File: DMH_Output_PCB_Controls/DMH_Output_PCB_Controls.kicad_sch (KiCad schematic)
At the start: 14 parts, among them J1 TS_Jack_6.35mm_Sw, J2 TS_Jack_6.35mm_Sw, J200 IDC_02x05, J21 Conn_01x02, J22 Conn_01x02, J24 Conn_01x02, J25 Conn_01x02, J3 TRS Jack 6.35mm, J4 TRS Jack 6.35mm, J5 TRS Jack 6.35mm, J6 TS_Jack_6.35mm_Sw, J7 TS_Jack_6.35mm_Sw, J8 TS_Jack_6.35mm_Sw, J9 TS_Jack_6.35mm_Sw

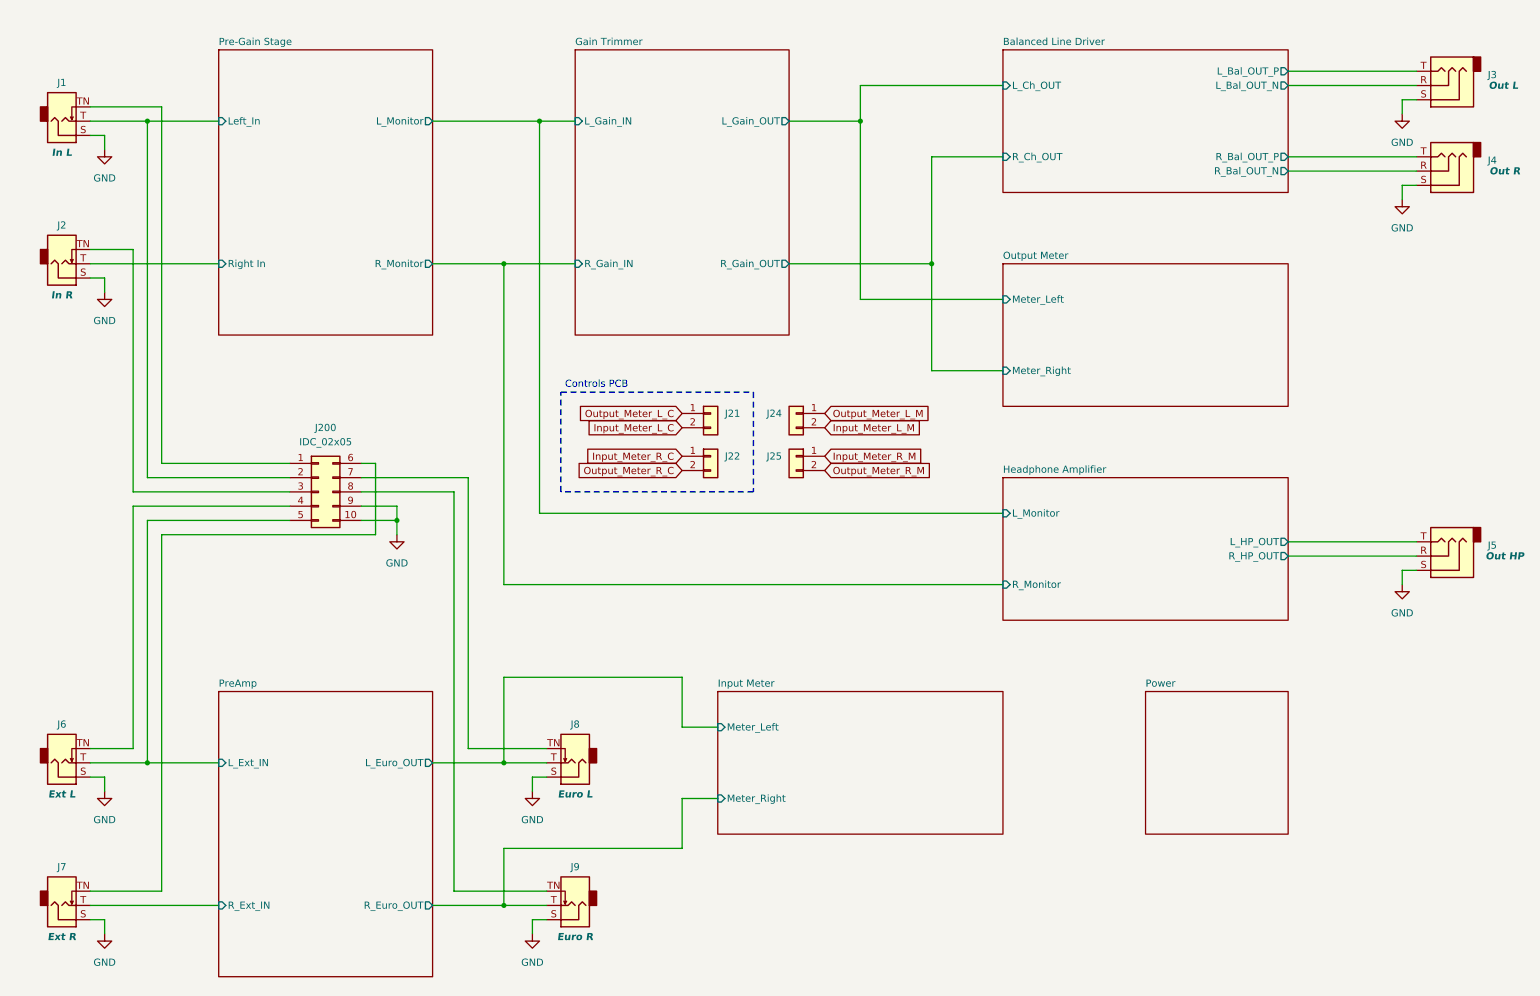
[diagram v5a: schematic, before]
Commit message: Replaced jack symbols with 5pin ones
Also updated Meter LED current source resistor to 75R
Also increased LED guiding PCB mounting holes to M2.5
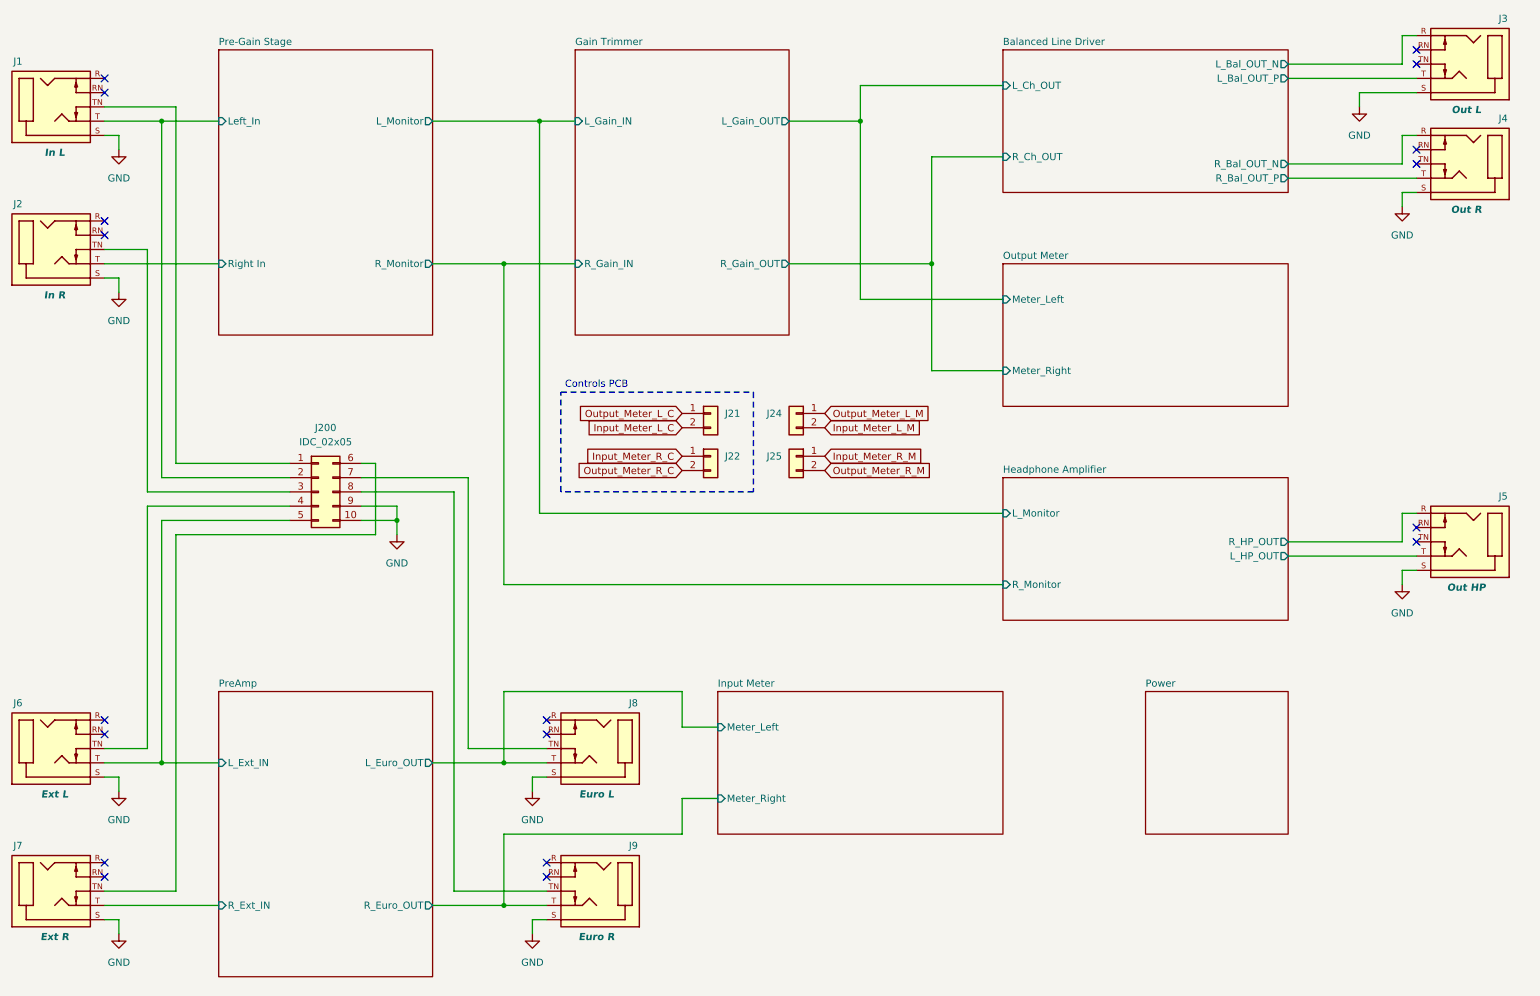
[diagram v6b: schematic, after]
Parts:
- removed J1, J2, J6, J7, J8, J9: TS_Jack_6.35mm_Sw, SynthStuff:CUI_MJ-63052A, symbol SynthStuff:TS_Jack_6.35mm_Sw
- removed J3, J4, J5: TRS Jack 6.35mm, SynthStuff:CUI_SJ-63083A, symbol Connector_Audio:AudioJack3
- added J1, J2, J3, J4, J5, J6, J7, J8, J9: TRS_Jack_6.35mm_Sw, SynthStuff:CUI_SJ-63083D, symbol SynthStuff:TRS_Jack_6.35mm_Sw
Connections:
- net Balanced Line Driver/L_Bal_OUT_N: now also J3.R (4)
- net Balanced Line Driver/L_Bal_OUT_P: now also J3.T (3)
- net Balanced Line Driver/R_Bal_OUT_N: now also J4.R (4)
- net Balanced Line Driver/R_Bal_OUT_P: now also J4.T (3)
- net GND: now also J1.S (1), J2.S (1), J3.S (1), J4.S (1), J5.S (1), J6.S (1), J7.S (1), J8.S (1), J9.S (1)
- net Headphone Amplifier/L_HP_OUT: now also J5.T (3)
- net Headphone Amplifier/R_HP_OUT: now also J5.R (4)
- net Input Meter/Meter_Left: now also J8.T (3)
- net Input Meter/Meter_Right: now also J9.T (3)
- net Pre-Gain Stage/Left_In: now also J1.T (3)
- net Pre-Gain Stage/Right In: now also J2.T (3)
- net PreAmp/L_Ext_IN: now also J6.T (3)
- net PreAmp/R_Ext_IN: now also J7.T (3)
- net at J200.7 (Pin_7): now also J8.TN (2)
- net at J200.3 (Pin_3): now also J2.TN (2)
- net at J200.6 (Pin_6): now also J7.TN (2)
- net at J200.4 (Pin_4): now also J6.TN (2)
- net at J200.8 (Pin_8): now also J9.TN (2)
- net at J200.1 (Pin_1): now also J1.TN (2)
- no-connect marks 0 -> 18

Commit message: Prep for Main and MZ PCBs design in progress
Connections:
- net GND: now also J200.5 (Pin_5); no longer J200.9 (Pin_9)
- net Pre-Gain Stage/Left_In: now also J200.6 (Pin_6); no longer J200.2 (Pin_2)
- net PreAmp/L_Ext_IN: now also J200.7 (Pin_7); no longer J200.5 (Pin_5)
- net at J7.TN (2): now also J200.2 (Pin_2); no longer J200.6 (Pin_6)
- net at J2.TN (2): now also J200.1 (Pin_1); no longer J200.3 (Pin_3)
- net at J9.TN (2): now also J200.9 (Pin_9); no longer J200.8 (Pin_8)
- net at J1.TN (2): now also J200.3 (Pin_3); no longer J200.1 (Pin_1)
- net at J8.TN (2): now also J200.8 (Pin_8); no longer J200.7 (Pin_7)

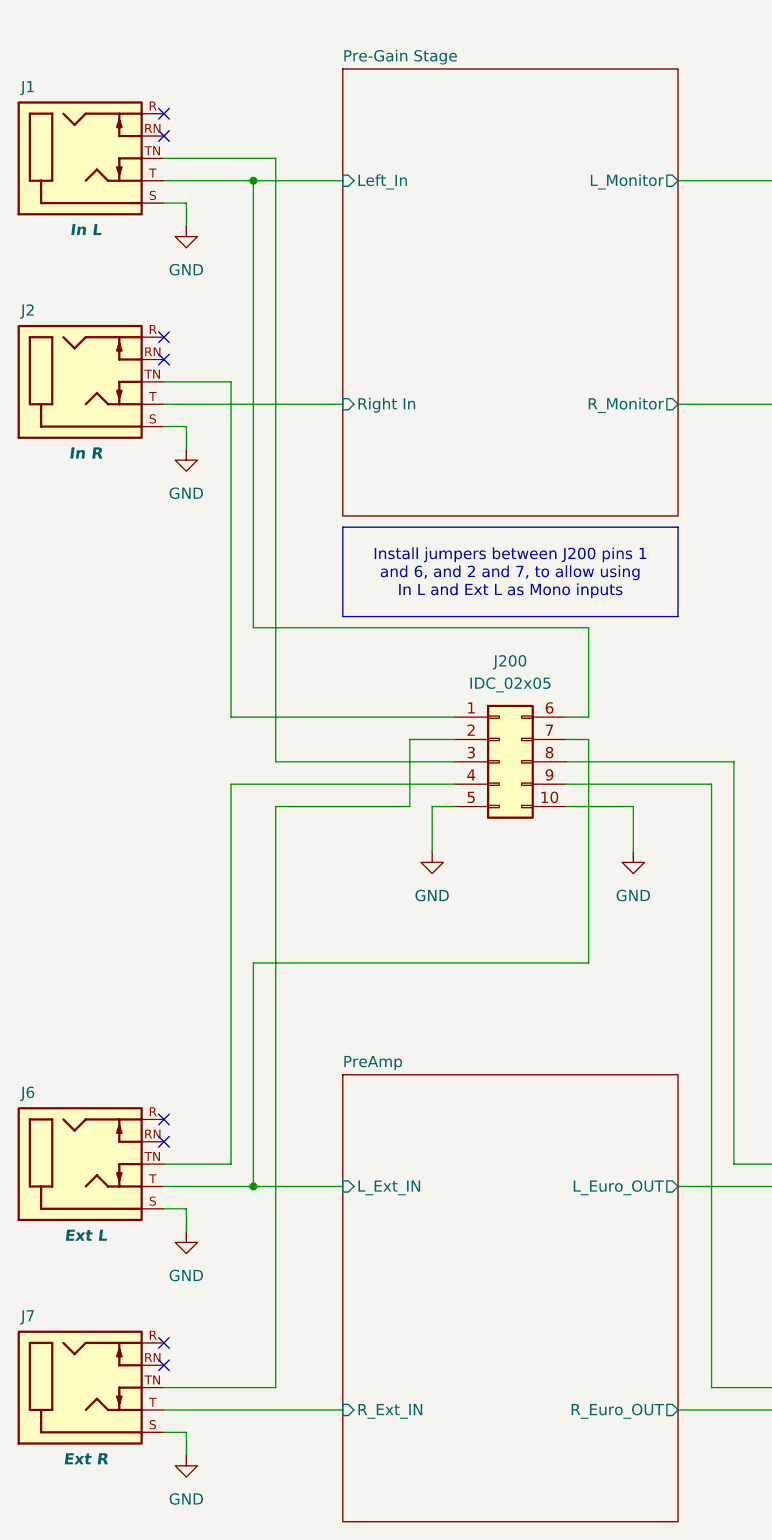
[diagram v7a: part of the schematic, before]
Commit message: Main PCB routing done
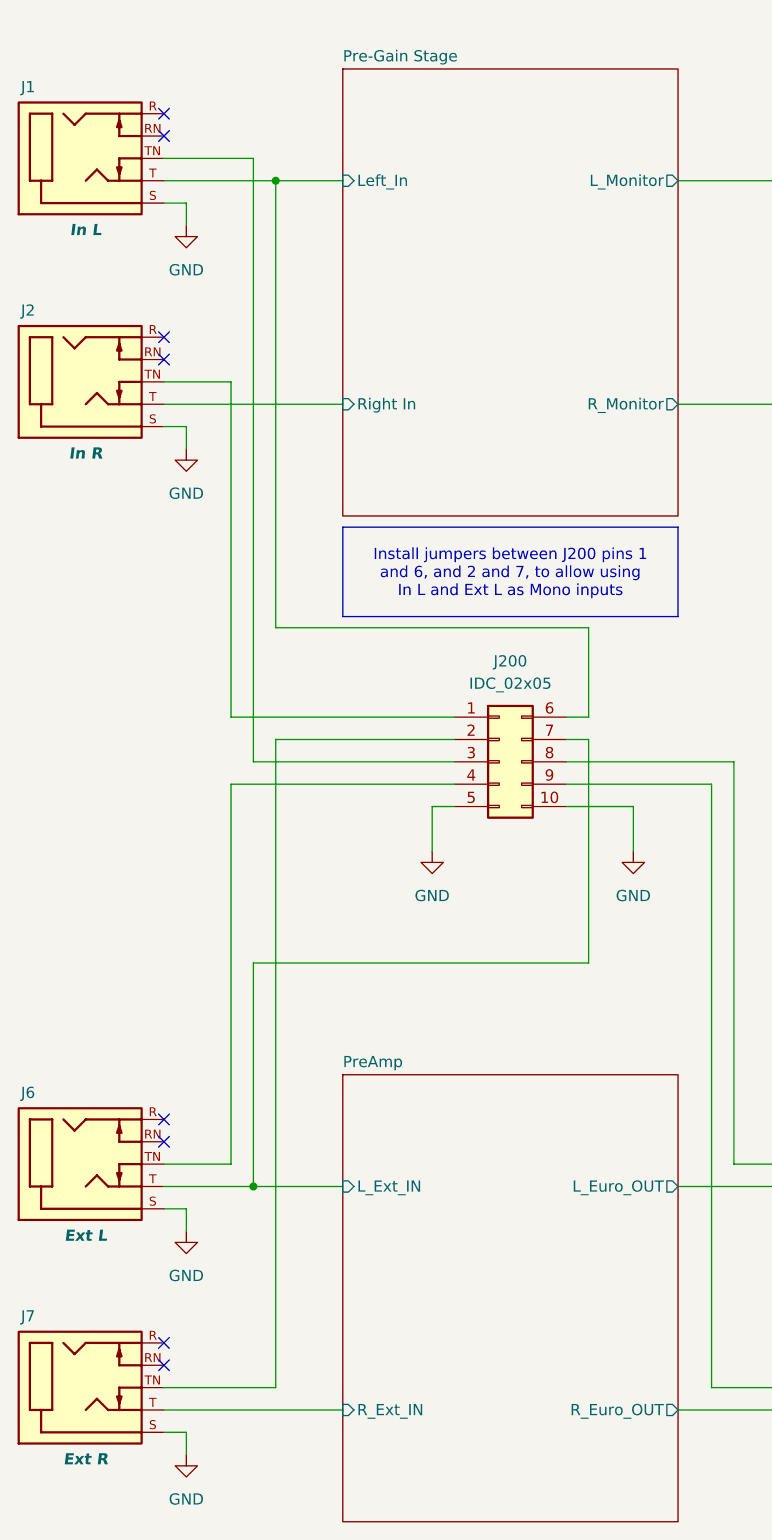
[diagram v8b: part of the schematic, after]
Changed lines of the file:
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@@
 	)
 	(junction
-		(at 40.64 38.1)
+		(at 43.18 38.1)
 		(diameter 0)
 		(color 0 0 0 0)
@@
 	(wire
 		(pts
-			(xy 30.48 38.1) (xy 40.64 38.1)
+			(xy 30.48 38.1) (xy 43.18 38.1)
 		)
 		(stroke
@@
 	(wire
 		(pts
-			(xy 58.42 109.22) (xy 58.42 101.6)
-		)
-		(stroke
-			(width 0)
-			(type default)
-		)
-	)
-	(wire
-		(pts
-			(xy 40.64 88.9) (xy 40.64 38.1)
+			(xy 43.18 88.9) (xy 43.18 38.1)
 		)
 		(stroke
@@
 	(wire
 		(pts
-			(xy 30.48 35.56) (xy 43.18 35.56)
-		)
-		(stroke
-			(width 0)
-			(type default)
-		)
-	)
-	(wire
-		(pts
-			(xy 43.18 35.56) (xy 43.18 104.14)
+			(xy 30.48 35.56) (xy 40.64 35.56)
+		)
+		(stroke
+			(width 0)
+			(type default)
+		)
+	)
+	(wire
+		(pts
+			(xy 40.64 35.56) (xy 40.64 104.14)
 		)
 		(stroke
@@
 	(wire
 		(pts
-			(xy 58.42 101.6) (xy 63.5 101.6)
-		)
-		(stroke
-			(width 0)
-			(type default)
-		)
-	)
-	(wire
-		(pts
 			(xy 106.68 154.94) (xy 109.22 154.94)
 		)
@@
 	(wire
 		(pts
-			(xy 43.18 109.22) (xy 58.42 109.22)
+			(xy 43.18 101.6) (xy 63.5 101.6)
 		)
 		(stroke
@@
 	(wire
 		(pts
-			(xy 43.18 104.14) (xy 63.5 104.14)
+			(xy 40.64 104.14) (xy 63.5 104.14)
 		)
 		(stroke
@@
 	(wire
 		(pts
-			(xy 40.64 38.1) (xy 50.8 38.1)
+			(xy 43.18 38.1) (xy 50.8 38.1)
 		)
 		(stroke
@@
 	(wire
 		(pts
-			(xy 78.74 88.9) (xy 40.64 88.9)
+			(xy 78.74 88.9) (xy 43.18 88.9)
 		)
 		(stroke
@@
 	(wire
 		(pts
-			(xy 43.18 175.26) (xy 43.18 109.22)
-		)
-		(stroke
+			(xy 43.18 175.26) (xy 43.18 101.6)
+		)
+		(stroke
